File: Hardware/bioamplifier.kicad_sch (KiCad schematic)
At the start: 41 parts, among them J1 Conn_01x07_Socket, J3 Conn_01x07_Socket, J4 Jumper, U1 ADS1299IPAG

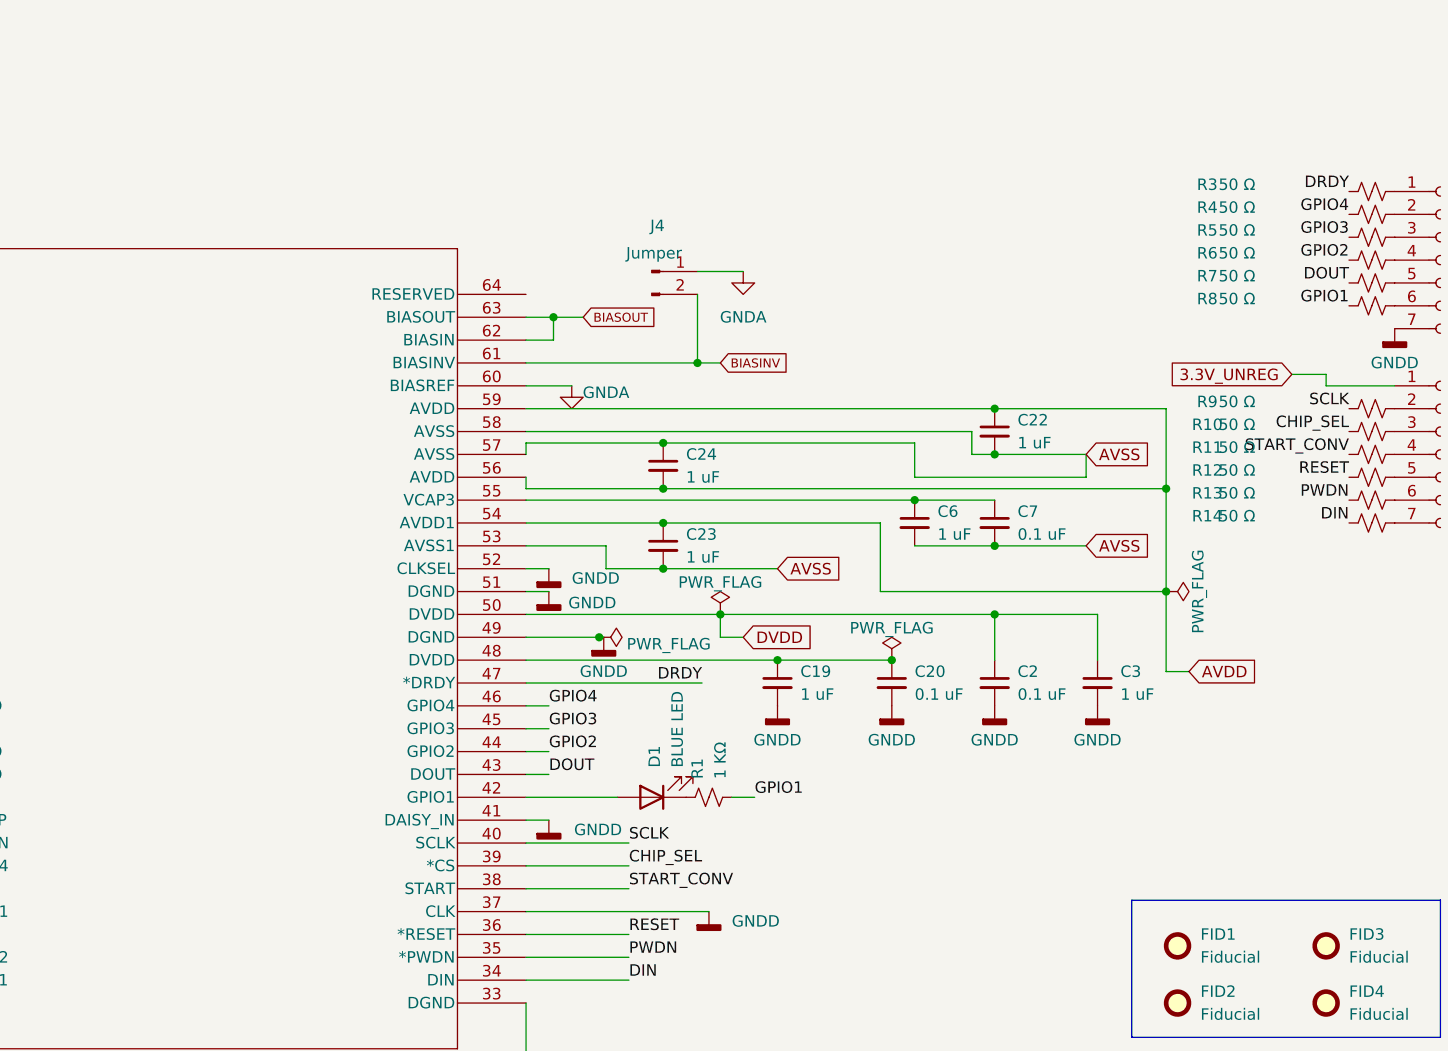
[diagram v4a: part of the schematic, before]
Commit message: Add Daisychain jumper
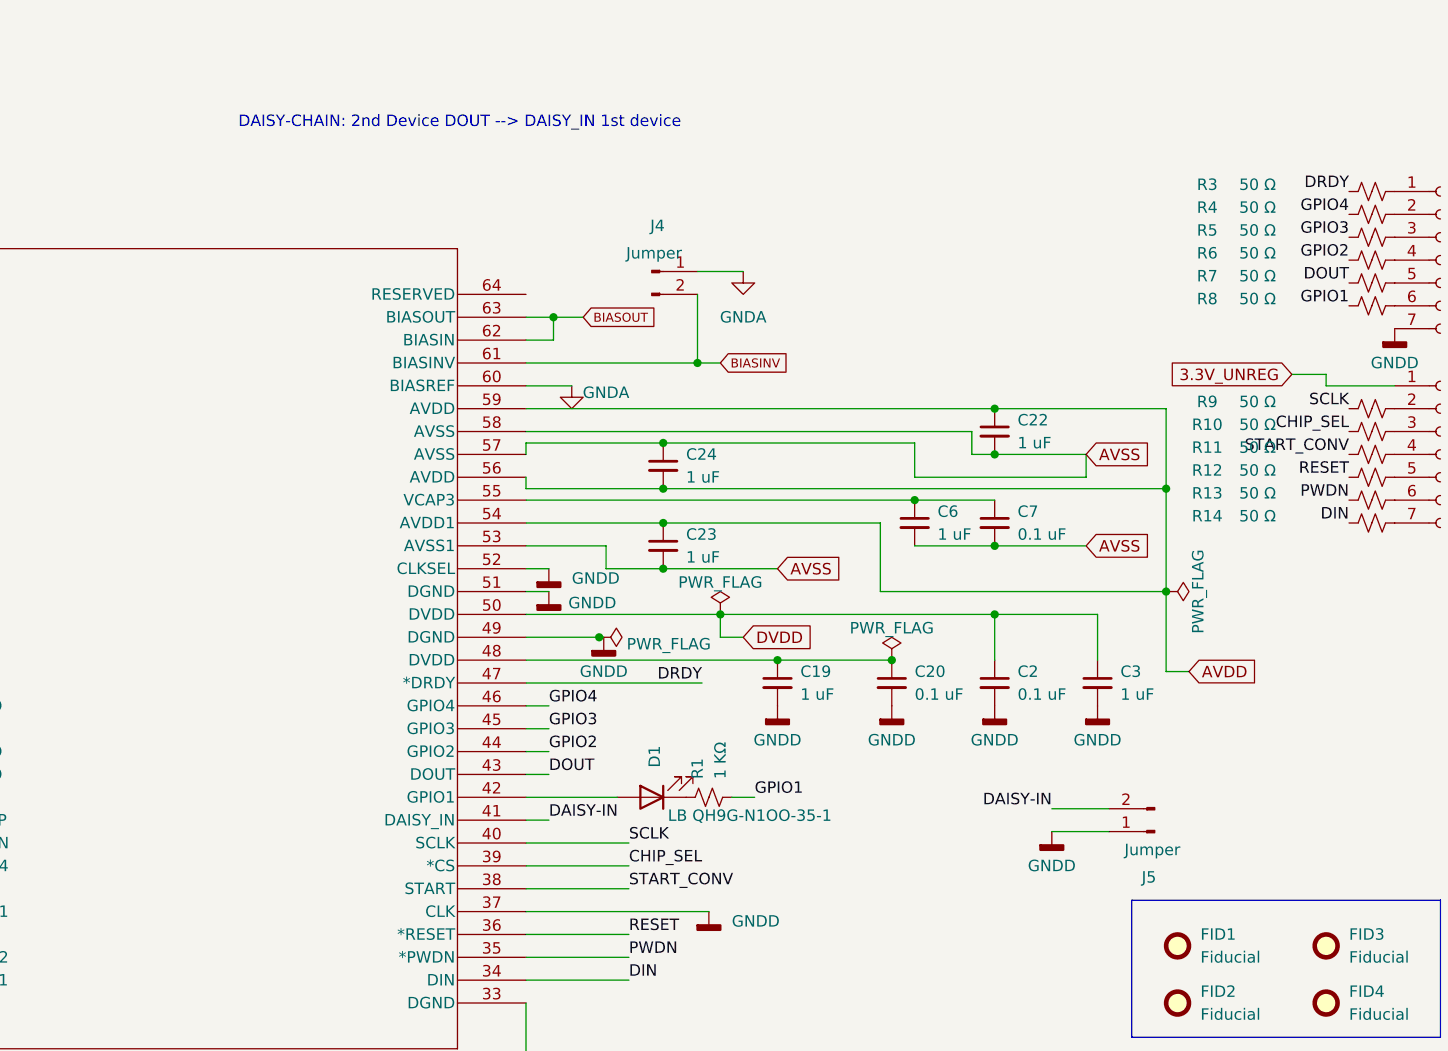
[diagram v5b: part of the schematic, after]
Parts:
- added J5: Jumper, Connector_PinHeader_2.54mm:PinHeader_1x02_P2.54mm_Vertical, symbol Connector:Conn_01x02_Pin
- D1: value BLUE LED -> LB QH9G-N1OO-35-1
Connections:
- net GNDD: now also J5.1 (Pin_1); no longer U1.41 (DAISY_IN)
- new net DAISY-IN: J5.2 (Pin_2), U1.41 (DAISY_IN)
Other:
- note added: "DAISY-CHAIN: 2nd Device DOUT --> DAISY_IN 1st device"
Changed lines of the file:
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@@
 		)
 	)
+	(text "DAISY-CHAIN: 2nd Device DOUT --> DAISY_IN 1st device\n"
+		(exclude_from_sim no)
+		(at 171.704 41.91 0)
+		(effects
+			(font
+				(face "FiraCode Nerd Font")
+				(size 1.27 1.27)
+			)
+		)
+	)
 	(junction
 		(at 92.71 139.7)
@@
 	(wire
 		(pts
+			(xy 237.49 120.65) (xy 243.84 120.65)
+		)
+		(stroke
+			(width 0)
+			(type default)
+		)
+	)
+	(wire
+		(pts
 			(xy 107.95 129.54) (xy 92.71 129.54)
 		)
@@
 	(wire
 		(pts
+			(xy 237.49 118.11) (xy 243.84 118.11)
+		)
+		(stroke
+			(width 0)
+			(type default)
+		)
+	)
+	(wire
+		(pts
 			(xy 179.07 106.68) (xy 181.61 106.68)
 		)
@@
 		)
 	)
+	(label "DAISY-IN"
+		(at 237.49 118.11 180)
+		(effects
+			(font
+				(size 1.27 1.27)
+			)
+			(justify right bottom)
+		)
+	)
 	(label "CHIP_SEL"
 		(at 190.5 124.46 0)
@@
 		)
 	)
+	(label "DAISY-IN"
+		(at 181.61 119.38 0)
+		(effects
+			(font
+				(size 1.27 1.27)
+			)
+			(justify left bottom)
+		)
+	)
 	(label "DRDY"
 		(at 270.51 49.53 180)
@@
 	)
 	(symbol
+		(lib_id "Connector:Conn_01x02_Pin")
+		(at 248.92 120.65 180)
+		(unit 1)
+		(exclude_from_sim no)
+		(in_bom yes)
+		(on_board yes)
+		(dnp no)
+		(property "Reference" "J5"
+			(at 248.285 125.73 0)
+			(effects
+				(font
+					(size 1.27 1.27)
+				)
+			)
+		)
+		(property "Value" "Jumper"
+			(at 248.666 122.682 0)
+			(effects
+				(font
+					(size 1.27 1.27)
+				)
+			)
+		)
+		(property "Footprint" "Connector_PinHeader_2.54mm:PinHeader_1x02_P2.54mm_Vertical"
+			(at 248.92 120.65 0)
+			(effects
+				(font
+					(size 1.27 1.27)
+				)
+				(hide yes)
+			)
+		)
+		(property "Datasheet" "~"
+			(at 248.92 120.65 0)
+			(effects
+				(font
+					(size 1.27 1.27)
+				)
+				(hide yes)
+			)
+		)
+		(property "Description" "Generic connector, single row, 01x02, script generated"
+			(at 248.92 120.65 0)
+			(effects
+				(font
+					(size 1.27 1.27)
+				)
+				(hide yes)
+			)
+		)
+		(pin "2"
+		)
+		(pin "1"
+		)
+		(instances
+			(project "bioamplifier"
+				(path "/59c54cdb-19a2-4654-a4c9-f1907d038780"
+					(reference "J5")
+					(unit 1)
+				)
+			)
+		)
+	)
+	(symbol
 		(lib_id "power:GNDD")
 		(at 219.71 106.68 0)
@@
 		)
 		(property "Value" "50 Ω"
-			(at 258.064 48.768 90)
+			(at 260.35 48.768 90)
 			(effects
 				(font
@@
 		)
 		(property "Value" "50 Ω"
-			(at 258.064 58.928 90)
+			(at 260.35 58.928 90)
 			(effects
 				(font
@@
 		)
 		(property "Value" "50 Ω"
-			(at 258.064 75.438 90)
+			(at 260.35 75.438 90)
 			(effects
 				(font
@@
 		)
 		(property "Value" "50 Ω"
-			(at 258.064 77.978 90)
+			(at 260.35 77.978 90)
 			(effects
 				(font
@@
 		)
 		(property "Value" "50 Ω"
-			(at 258.064 80.518 90)
+			(at 260.35 80.518 90)
 			(effects
 				(font
@@
 		)
 		(property "Value" "50 Ω"
-			(at 258.064 72.898 90)
+			(at 260.35 72.898 90)
 			(effects
 				(font
@@
 		)
 		(property "Value" "50 Ω"
-			(at 258.064 83.058 90)
+			(at 260.35 83.058 90)
 			(effects
 				(font
@@
 		)
 		(property "Value" "50 Ω"
-			(at 258.064 51.308 90)
+			(at 260.35 51.308 90)
 			(effects
 				(font
@@
 		)
 		(property "Value" "50 Ω"
-			(at 258.064 85.598 90)
+			(at 260.35 85.598 90)
 			(do_not_autoplace yes)
 			(effects
@@
 	)
 	(symbol
+		(lib_id "power:GNDD")
+		(at 237.49 120.65 0)
+		(unit 1)
+		(exclude_from_sim no)
+		(in_bom yes)
+		(on_board yes)
+		(dnp no)
+		(fields_autoplaced yes)
+		(property "Reference" "#PWR05"
+			(at 237.49 127 0)
+			(effects
+				(font
+					(size 1.27 1.27)
+				)
+				(hide yes)
+			)
+		)
+		(property "Value" "GNDD"
+			(at 237.49 124.46 0)
+			(effects
+				(font
+					(size 1.27 1.27)
+				)
+			)
+		)
+		(property "Footprint" ""
+			(at 237.49 120.65 0)
+			(effects
+				(font
+					(size 1.27 1.27)
+				)
+				(hide yes)
+			)
+		)
+		(property "Datasheet" ""
+			(at 237.49 120.65 0)
+			(effects
+				(font
+					(size 1.27 1.27)
+				)
+				(hide yes)
+			)
+		)
+		(property "Description" ""
+			(at 237.49 120.65 0)
+			(effects
+				(font
+					(size 1.27 1.27)
+				)
+				(hide yes)
+			)
+		)
+		(pin "1"
+		)
+		(instances
+			(project "bioamplifier"
+				(path "/59c54cdb-19a2-4654-a4c9-f1907d038780"
+					(reference "#PWR05")
+					(unit 1)
+				)
+			)
+		)
+	)
+	(symbol
 		(lib_id "Mechanical:MountingHole")
 		(at 265.43 153.67 0)
@@
 		)
 		(property "Value" "50 Ω"
-			(at 258.064 61.468 90)
+			(at 260.35 61.468 90)
 			(effects
 				(font
@@
 	)
 	(symbol
-		(lib_id "power:GNDD")
-		(at 181.61 119.38 0)
-		(unit 1)
-		(exclude_from_sim no)
-		(in_bom yes)
-		(on_board yes)
-		(dnp no)
-		(fields_autoplaced yes)
-		(property "Reference" "#PWR05"
-			(at 181.61 125.73 0)
-			(effects
-				(font
-					(size 1.27 1.27)
-				)
-				(hide yes)
-			)
-		)
-		(property "Value" "GNDD"
-			(at 184.404 120.4594 0)
-			(effects
-				(font
-					(size 1.27 1.27)
-				)
-				(justify left)
-			)
-		)
-		(property "Footprint" ""
-			(at 181.61 119.38 0)
-			(effects
-				(font
-					(size 1.27 1.27)
-				)
-				(hide yes)
-			)
-		)
-		(property "Datasheet" ""
-			(at 181.61 119.38 0)
-			(effects
-				(font
-					(size 1.27 1.27)
-				)
-				(hide yes)
-			)
-		)
-		(property "Description" ""
-			(at 181.61 119.38 0)
-			(effects
-				(font
-					(size 1.27 1.27)
-				)
-				(hide yes)
-			)
-		)
-		(pin "1"
-		)
-		(instances
-			(project "bioamplifier"
-				(path "/59c54cdb-19a2-4654-a4c9-f1907d038780"
-					(reference "#PWR05")
-					(unit 1)
-				)
-			)
-		)
-	)
-	(symbol
 		(lib_id "Device:LED")
 		(at 193.04 116.84 180)
@@
 		(on_board yes)
 		(dnp no)
-		(fields_autoplaced yes)
 		(property "Reference" "D1"
 			(at 193.3575 113.538 90)
@@
 			)
 		)
-		(property "Value" "BLUE LED"
-			(at 195.8975 113.538 90)
+		(property "Value" "LB QH9G-N1OO-35-1"
+			(at 194.818 118.872 0)
 			(effects
 				(font
@@
 		)
 		(property "Value" "50 Ω"
-			(at 258.064 56.388 90)
+			(at 260.35 56.388 90)
 			(effects
 				(font
@@
 		)
 		(property "Value" "50 Ω"
-			(at 258.064 53.848 90)
+			(at 260.35 53.848 90)
 			(effects
 				(font

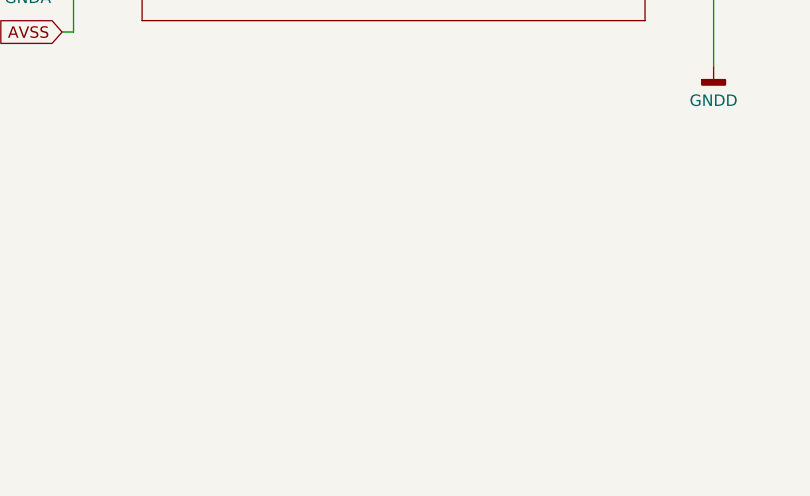
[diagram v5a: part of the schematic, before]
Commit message: Add poweron Led
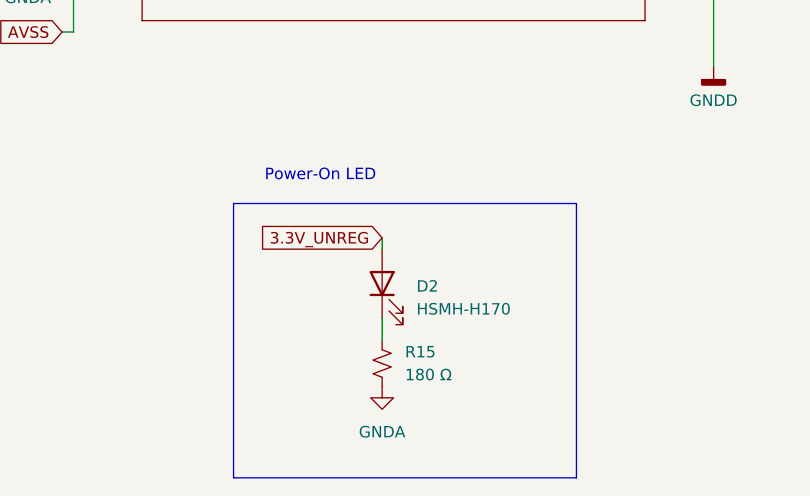
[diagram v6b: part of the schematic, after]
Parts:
- added D2: HSMH-H170, LED_SMD:LED_0805_2012Metric, symbol Device:LED
- added R15: 180 Ω, Resistor_SMD:R_0603_1608Metric, symbol Device:R_Small_US
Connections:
- net 3.3V_UNREG: now also D2.2 (A)
- net GNDA: now also R15.2
- new net: D2.1 (K), R15.1
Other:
- note added: "Power-On LED"

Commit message: TODO: GND pours & planes separation
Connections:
- net GNDD is gone; now on net GNDA: C1.2, C19.2, C2.2, C20.2, C3.2, J3.7 (Pin_7), J5.1 (Pin_1), U1.23 (AVSS), U1.33 (DGND), U1.37 (CLK), U1.49 (DGND), U1.51 (DGND), U1.52 (CLKSEL)
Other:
- note added: "SPI HEADERS"
- moved on the sheet: J1, J3, R10, R11, R12, R13, R14, R3, R4, R5, R6, R7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

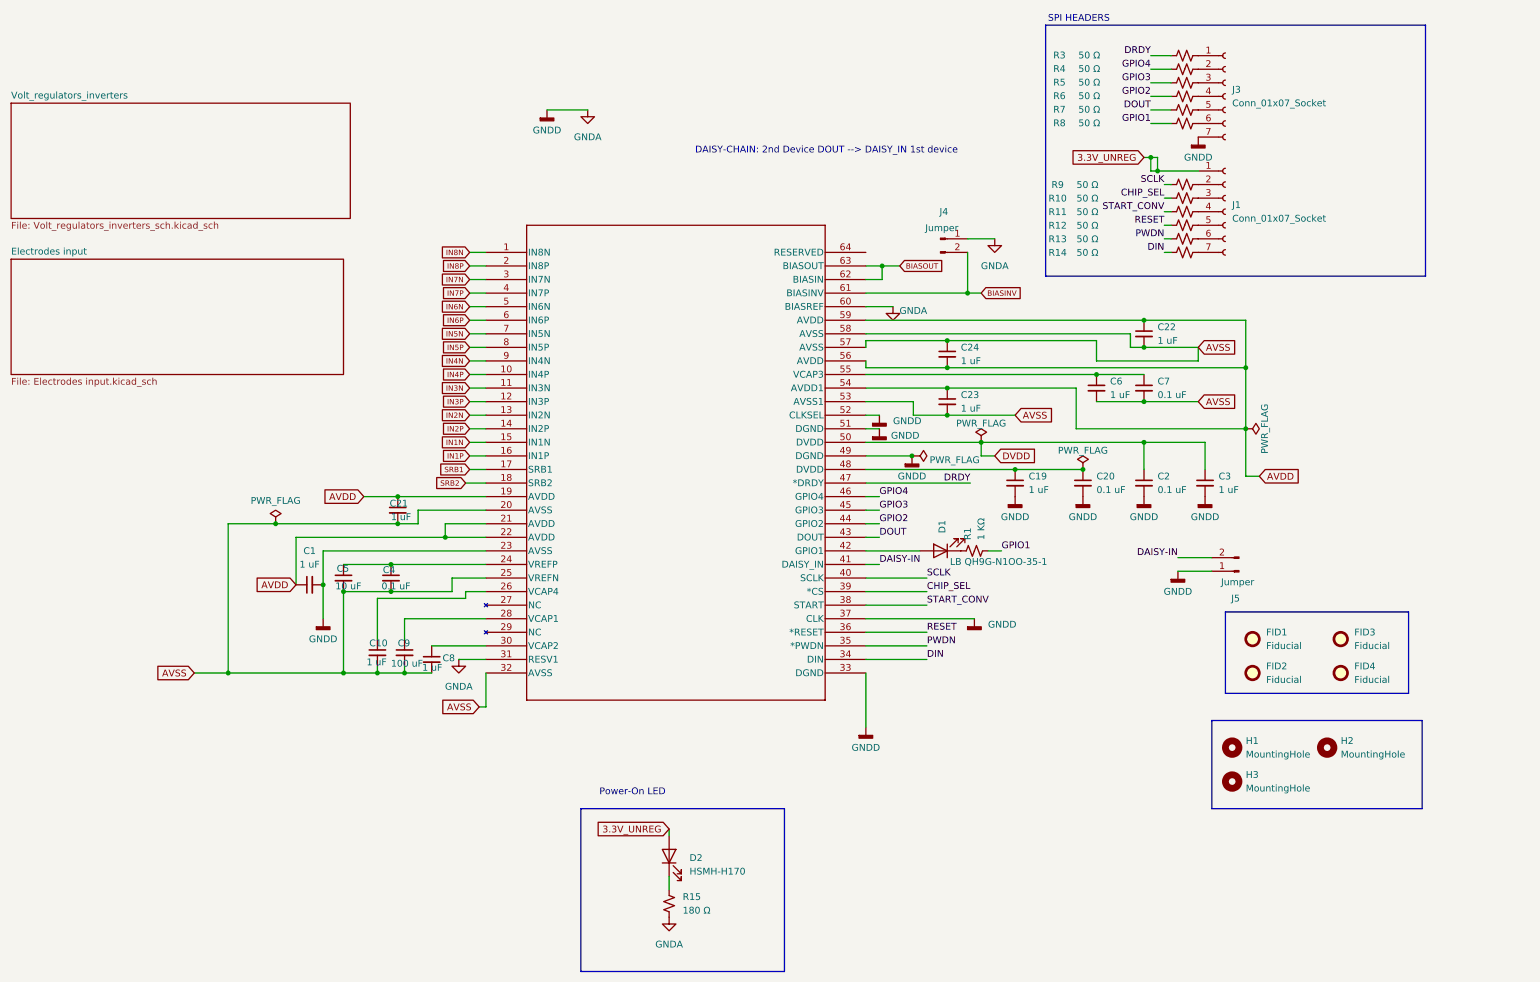
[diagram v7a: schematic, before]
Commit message: Fix GndA Avss connection, standardize grids
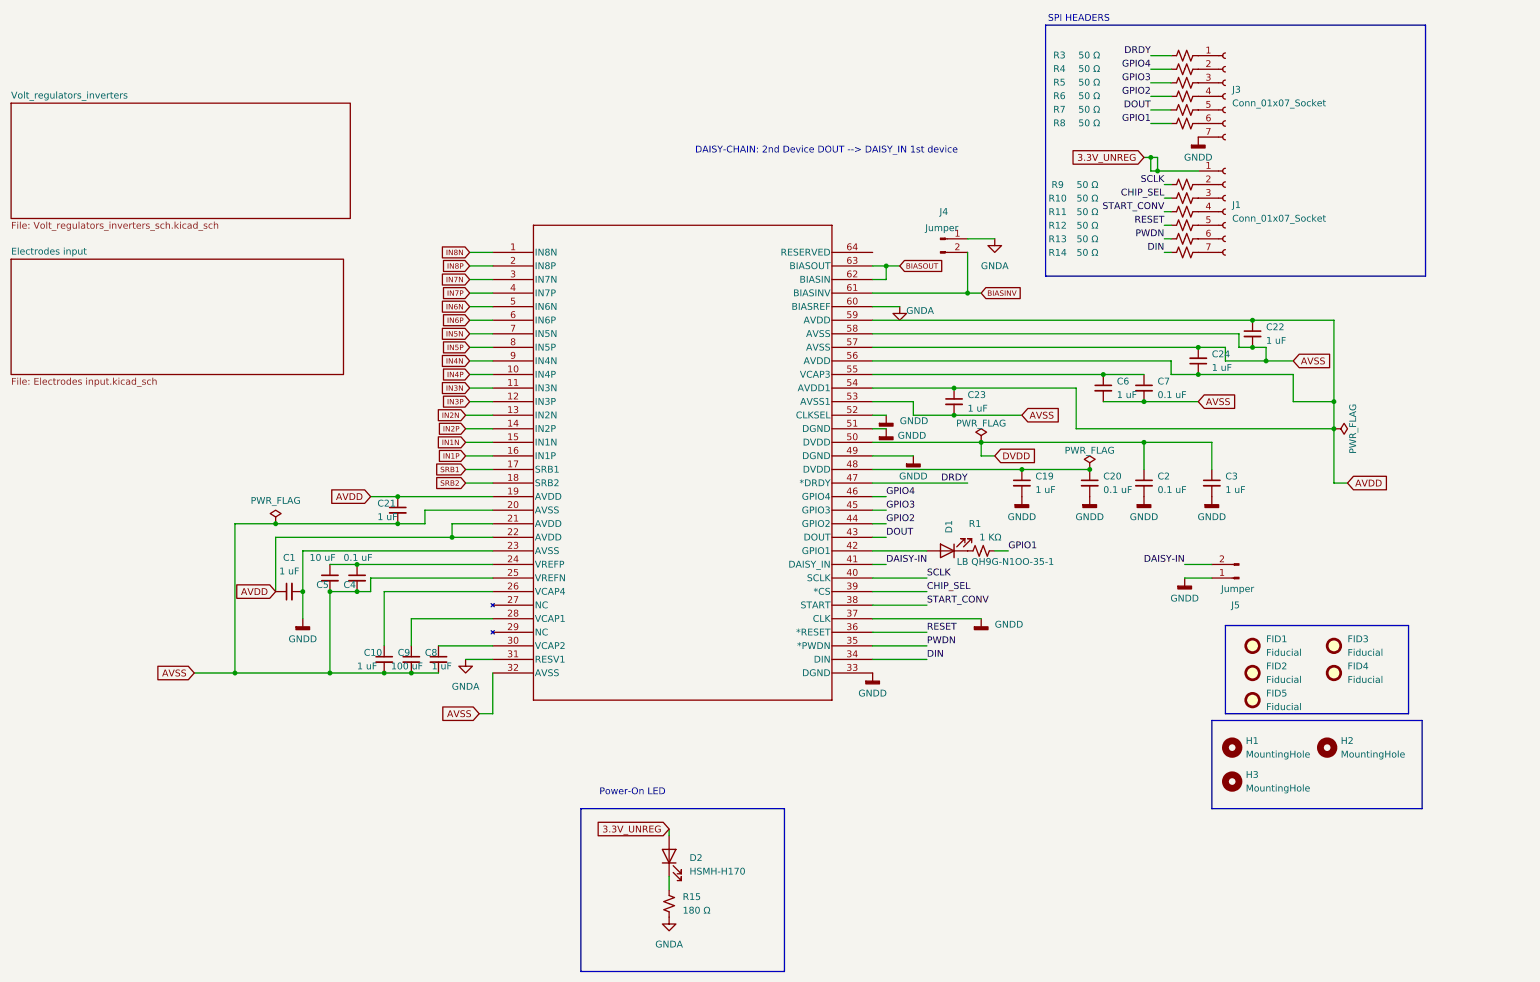
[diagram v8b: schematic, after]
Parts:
- added FID5: Fiducial, Fiducial:Fiducial_1mm_Mask3mm, symbol Mechanical:Fiducial
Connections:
- net AVDD: now also C24.1; no longer C24.2
- net AVSS: now also C24.2; no longer C24.1
- net GNDA: no longer C1.2, C19.2, C2.2, C20.2, C3.2, J3.7 (Pin_7), J5.1 (Pin_1), U1.23 (AVSS), U1.33 (DGND), U1.37 (CLK), U1.49 (DGND), U1.51 (DGND), U1.52 (CLKSEL)
- new net GNDD: C1.2, C19.2, C2.2, C20.2, C3.2, J3.7 (Pin_7), J5.1 (Pin_1), U1.23 (AVSS), U1.33 (DGND), U1.37 (CLK), U1.49 (DGND), U1.51 (DGND), U1.52 (CLKSEL)
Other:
- moved on the sheet: C1, C10, C19, C20, C22, C23, C24, C3, C4, C5, C6, C8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
